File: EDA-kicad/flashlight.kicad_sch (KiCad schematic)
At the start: 3 parts, among them U5 Flash-LED-Lumiled

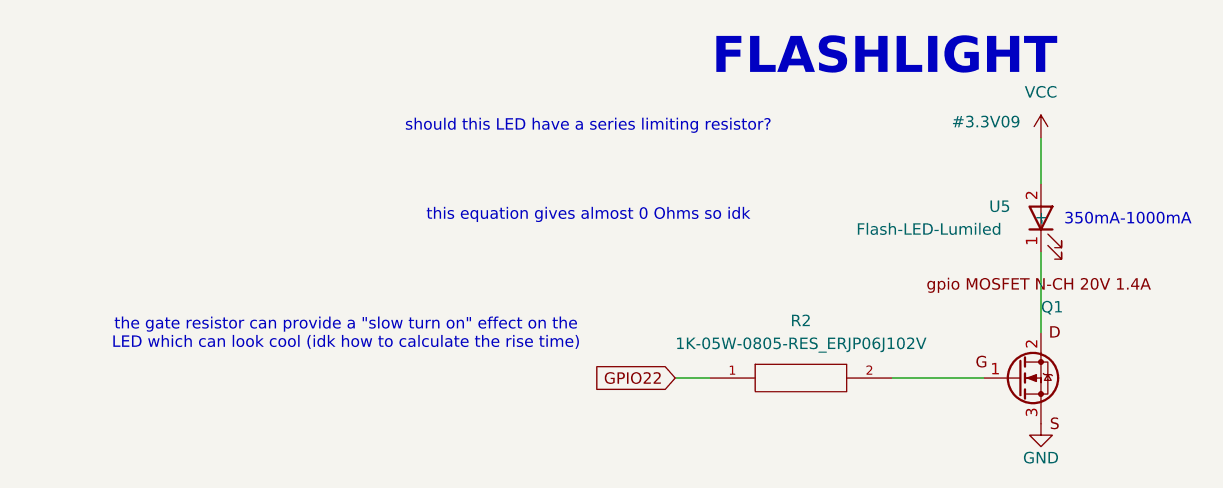
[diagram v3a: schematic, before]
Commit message: added footprints to transistors
used the footprint assigned to Q1

check my work
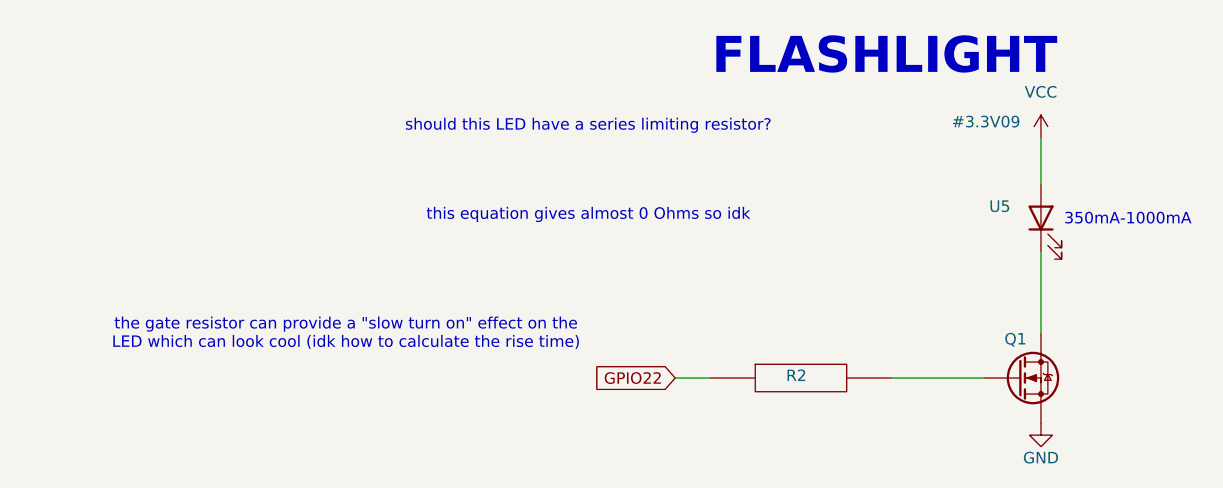
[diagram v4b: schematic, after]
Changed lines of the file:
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@@
 					(size 1.27 1.27)
 				)
+				(hide yes)
 			)
 		)
@@
 		(on_board yes)
 		(dnp no)
-		(fields_autoplaced yes)
 		(property "Reference" "R2"
-			(at 143.51 97.79 0)
+			(at 143.002 103.886 0)
 			(effects
 				(font
@@
 					(size 1.27 1.27)
 				)
+				(hide yes)
 			)
 		)
@@
 		(dnp no)
 		(property "Reference" "Q1"
-			(at 170.18 96.266 0)
+			(at 166.116 99.822 0)
 			(effects
 				(font
@@
 				)
 				(justify left)
-			)
-		)
+				(hide yes)
+			)
+		)
